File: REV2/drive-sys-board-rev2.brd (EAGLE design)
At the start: 109.2 x 48.3 mm, 28 parts

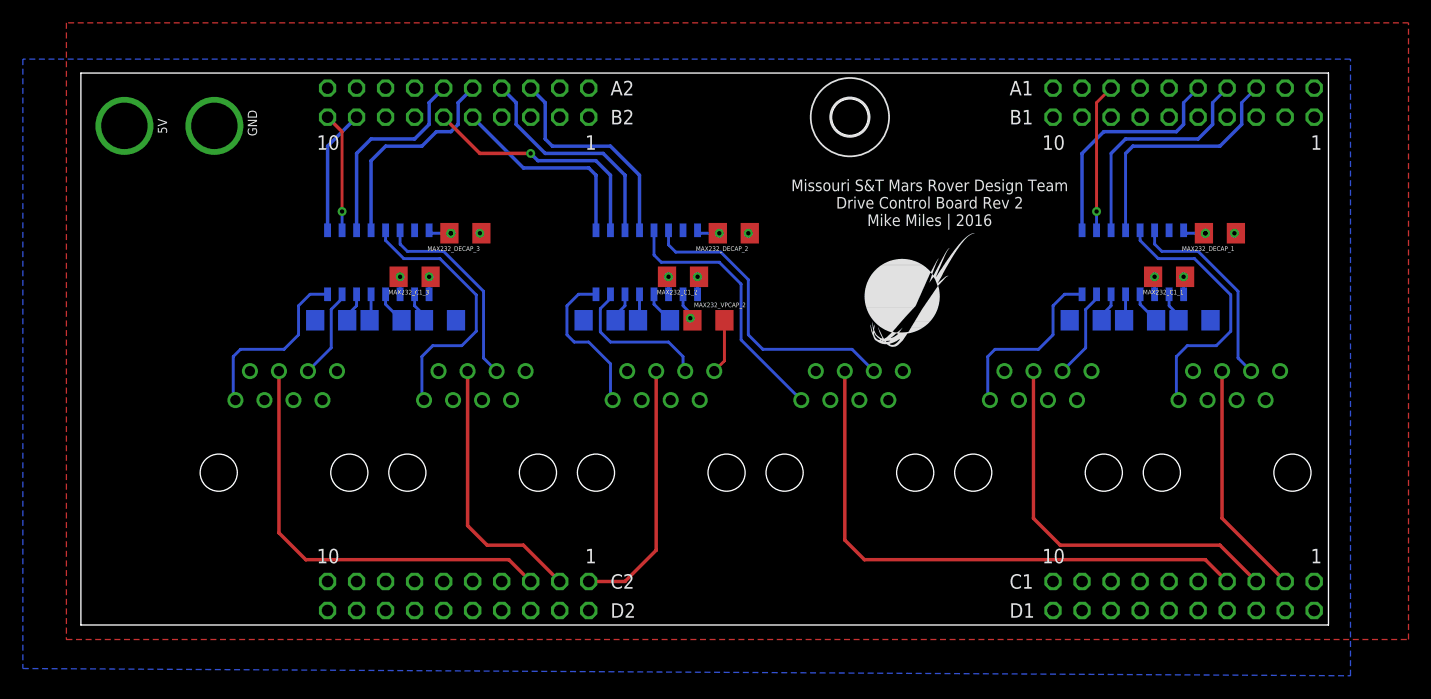
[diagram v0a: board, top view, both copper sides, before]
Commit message: adjusted board dims, regen'ed gerbers
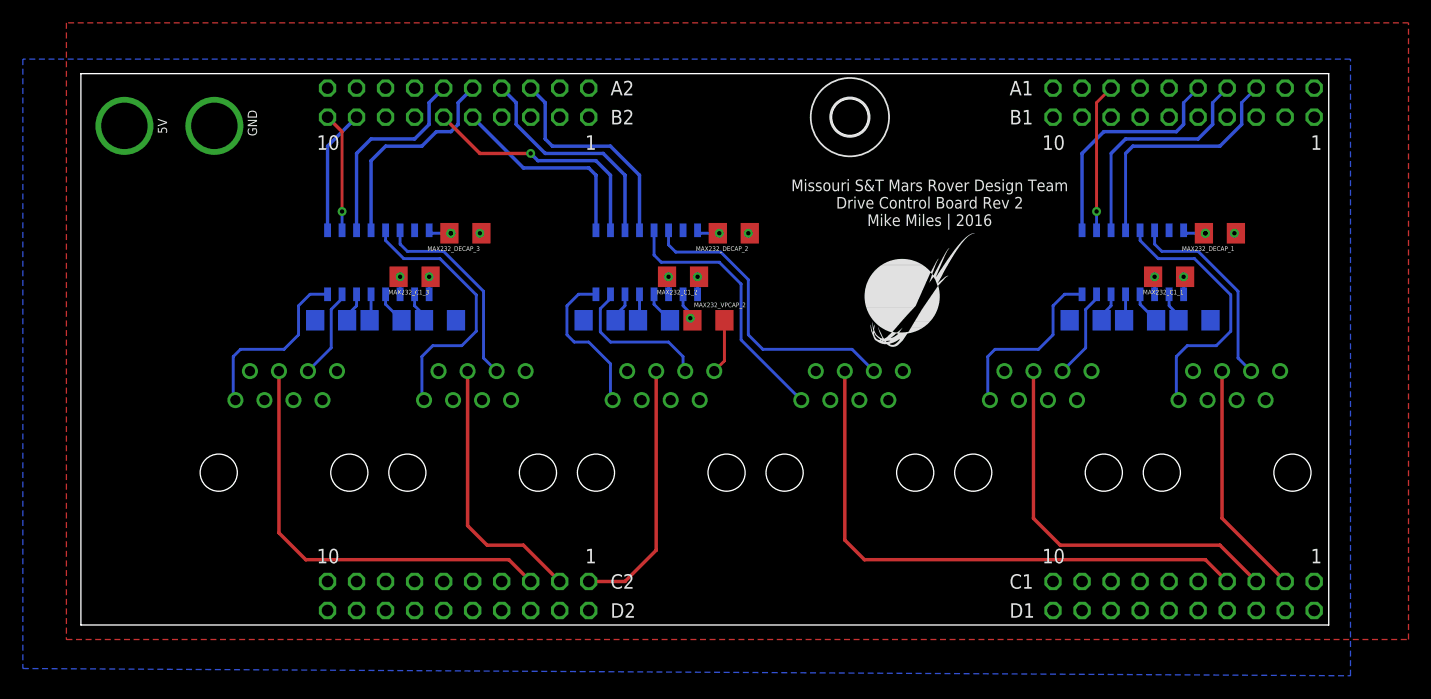
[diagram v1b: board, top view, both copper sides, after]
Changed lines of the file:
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@@
 <layer number="16" name="Bottom" color="1" fill="1" visible="yes" active="yes"/>
 <layer number="17" name="Pads" color="2" fill="1" visible="yes" active="yes"/>
-<layer number="18" name="Vias" color="2" fill="1" visible="no" active="yes"/>
-<layer number="19" name="Unrouted" color="6" fill="1" visible="no" active="yes"/>
-<layer number="20" name="Dimension" color="15" fill="1" visible="no" active="yes"/>
+<layer number="18" name="Vias" color="2" fill="1" visible="yes" active="yes"/>
+<layer number="19" name="Unrouted" color="6" fill="1" visible="yes" active="yes"/>
+<layer number="20" name="Dimension" color="13" fill="1" visible="yes" active="yes"/>
 <layer number="21" name="tPlace" color="7" fill="1" visible="yes" active="yes"/>
 <layer number="22" name="bPlace" color="7" fill="1" visible="no" active="yes"/>
@@
 <layer number="45" name="Holes" color="7" fill="1" visible="no" active="yes"/>
 <layer number="46" name="Milling" color="3" fill="1" visible="no" active="yes"/>
-<layer number="47" name="Measures" color="7" fill="1" visible="no" active="yes"/>
+<layer number="47" name="Measures" color="7" fill="1" visible="yes" active="yes"/>
 <layer number="48" name="Document" color="7" fill="1" visible="no" active="yes"/>
-<layer number="49" name="Reference" color="7" fill="1" visible="no" active="yes"/>
+<layer number="49" name="Reference" color="7" fill="1" visible="yes" active="yes"/>
 <layer number="50" name="dxf" color="7" fill="1" visible="no" active="yes"/>
-<layer number="51" name="tDocu" color="7" fill="1" visible="no" active="yes"/>
-<layer number="52" name="bDocu" color="7" fill="1" visible="no" active="yes"/>
+<layer number="51" name="tDocu" color="7" fill="1" visible="yes" active="yes"/>
+<layer number="52" name="bDocu" color="7" fill="1" visible="yes" active="yes"/>
 <layer number="91" name="Nets" color="2" fill="1" visible="no" active="no"/>
 <layer number="92" name="Busses" color="1" fill="1" visible="no" active="no"/>
@@
 <board>
 <plain>
-<wire x1="0" y1="0" x2="109.2" y2="0" width="0" layer="20"/>
-<wire x1="109.2" y1="0" x2="109.2" y2="48.311" width="0" layer="20"/>
-<wire x1="109.2" y1="48.311" x2="0" y2="48.311" width="0" layer="20"/>
-<wire x1="0" y1="48.311" x2="0" y2="0" width="0" layer="20"/>
+<wire x1="0" y1="0" x2="109.22" y2="0" width="0" layer="20"/>
+<wire x1="109.22" y1="0" x2="109.22" y2="48.26" width="0" layer="20"/>
+<wire x1="109.22" y1="48.26" x2="0" y2="48.26" width="0" layer="20"/>
+<wire x1="0" y1="48.26" x2="0" y2="0" width="0" layer="20"/>
 <text x="74.295" y="34.925" size="1.016" layer="21" align="bottom-center">Missouri S&amp;T Mars Rover Design Team
 Drive Control Board Rev 2
 Mike Miles | 2016</text>
+<dimension x1="0" y1="0" x2="109.22" y2="0" x3="54.61" y3="-12.065" textsize="1.778" layer="47" dtype="horizontal" unit="inch" precision="6" visible="yes"/>
+<dimension x1="109.22" y1="0" x2="109.22" y2="48.26" x3="124.46" y3="24.13" textsize="1.778" layer="47" dtype="horizontal" unit="inch" precision="6" visible="yes"/>
 </plain>
 <attributes>
